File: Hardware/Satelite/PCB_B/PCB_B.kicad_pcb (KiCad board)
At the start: 2 copper layers, 54 x 54 mm, 66 parts, among them IC1 MCP1642B-50I_MS, IC2 MCP1642B-50I_MS, J1 Conector_PCB_B-C, J2 Conector_PCB_A-B, U1 MIC5323-3.3YD5_TR, U2 ADP2108AUJ-3.3, U3 INA194, U4 MCP6001-OT, U5 INA194, U6 MCP6001-OT, U7 INA194, U8 BQ24091DGQT, U9 BQ27441DRZR-G1A

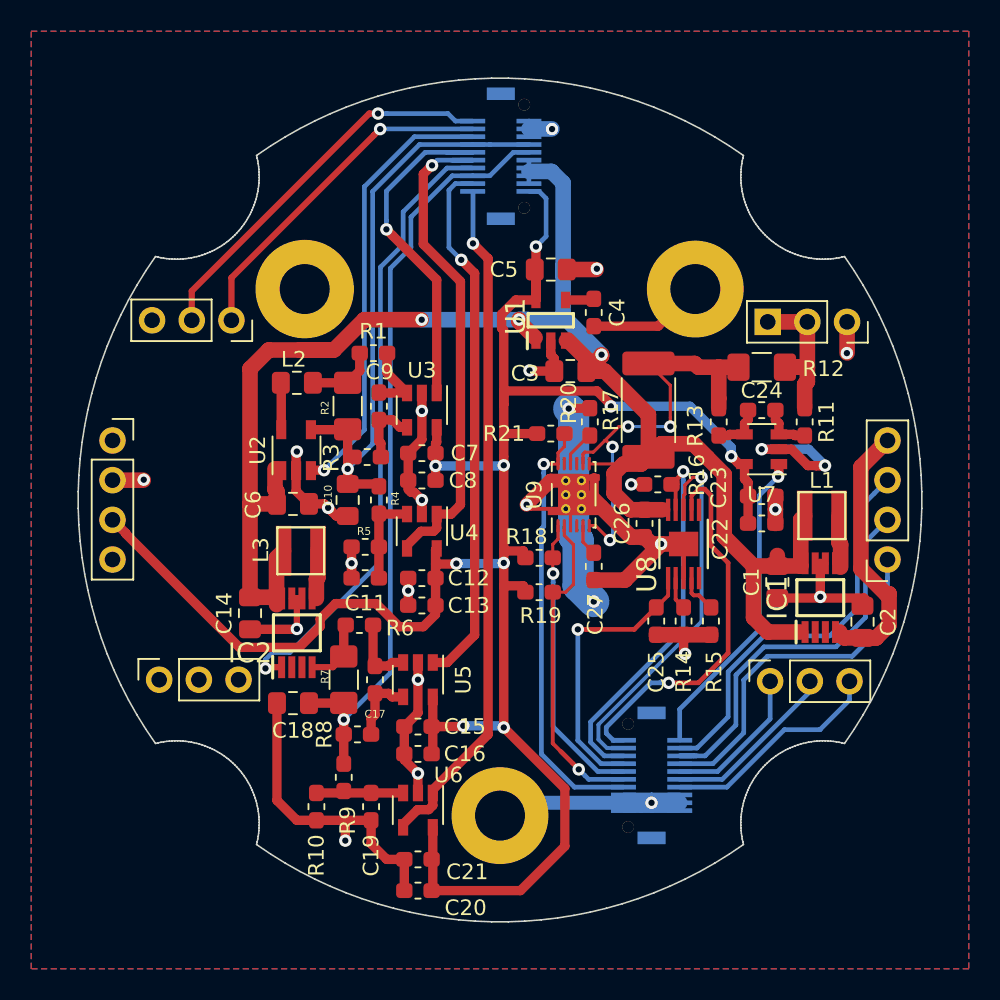
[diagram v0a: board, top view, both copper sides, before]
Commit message: Correciones de anchos de trazas en PCB B
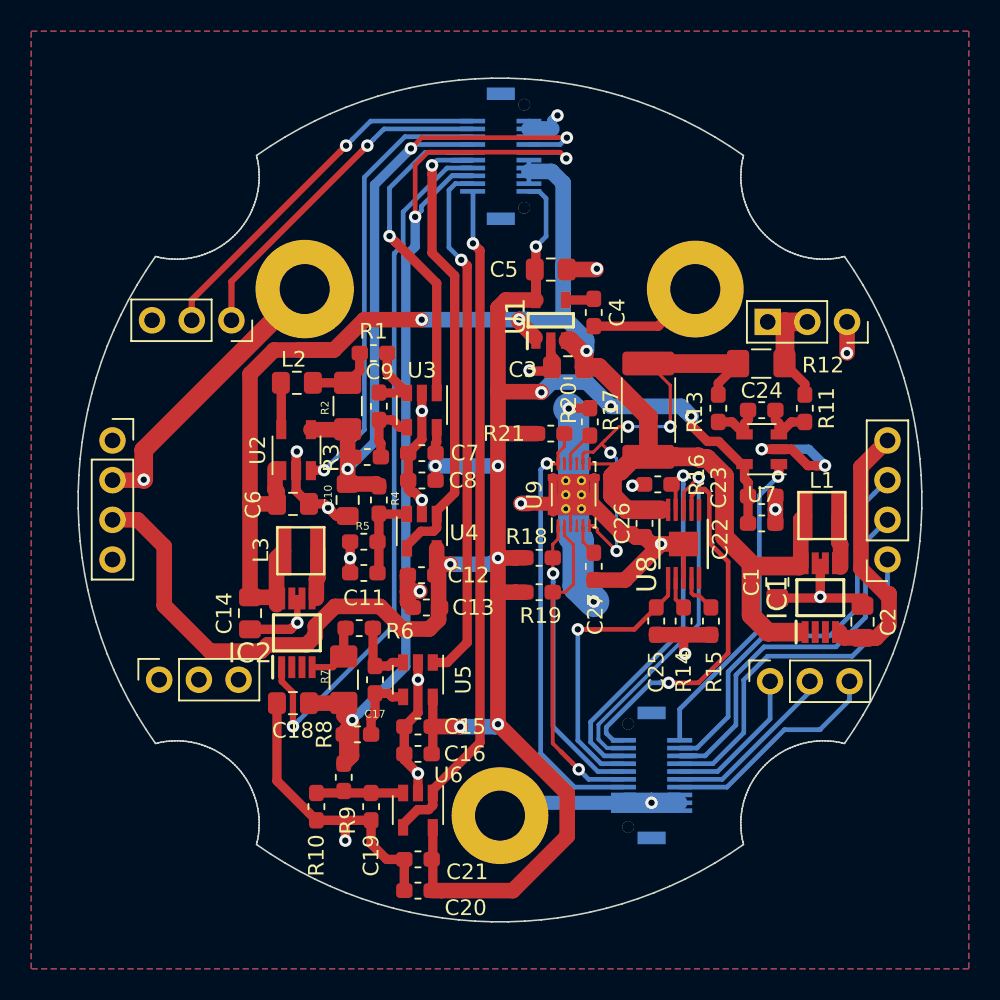
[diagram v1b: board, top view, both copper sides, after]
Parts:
- moved R13 0.87 mm to (14.0, -5.87)
- moved R11 0.87 mm to (19.5, -5.87)
- moved C11 0.34 mm to (-8.71, 4.67)
- moved R5 0.34 mm to (-8.71, 2.67)
- moved C13 0.32 mm to (-4.71, 6.88)
- moved C3 0.28 mm to (4.35, -8.49)
- moved R12 0.23 mm to (16.7, -8.73)
- moved R6 0.20 mm to (-9.01, 8.20)
- moved C12 0.19 mm to (-5.02, 4.81)
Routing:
- net GND: track 179.7 -> 199.0 mm
- net +5V: track 49.3 -> 66.5 mm, vias 1 -> 3
- net +3V3: track 38.0 -> 50.9 mm, vias 1 -> 3
- net +BATT: track 122.7 -> 114.3 mm
- net /ENABLE_5V: track 40.2 -> 45.5 mm
- net +3V3_Internal: track 140.7 -> 145.0 mm, vias 9 -> 10
- net /BATT_INTERNO: track 9.57 -> 7.97 mm
- net /Fuel Gauge/VBAT: track 28.7 -> 30.1 mm
- net /V_SENSE_3V3: track 32.2 -> 30.9 mm
- net /GPS_TX: track 24.8 -> 24.0 mm

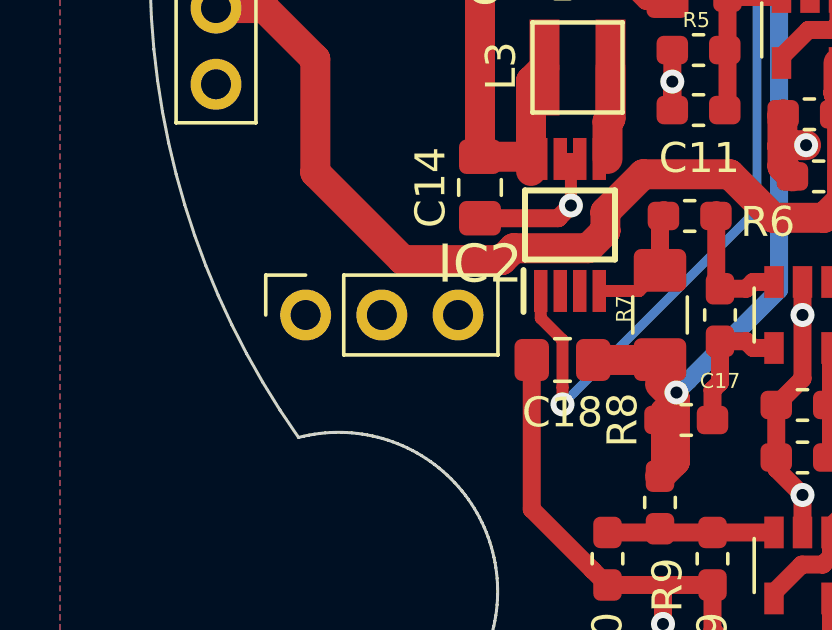
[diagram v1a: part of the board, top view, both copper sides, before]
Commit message: Eliminados pines no usados del conector A-B
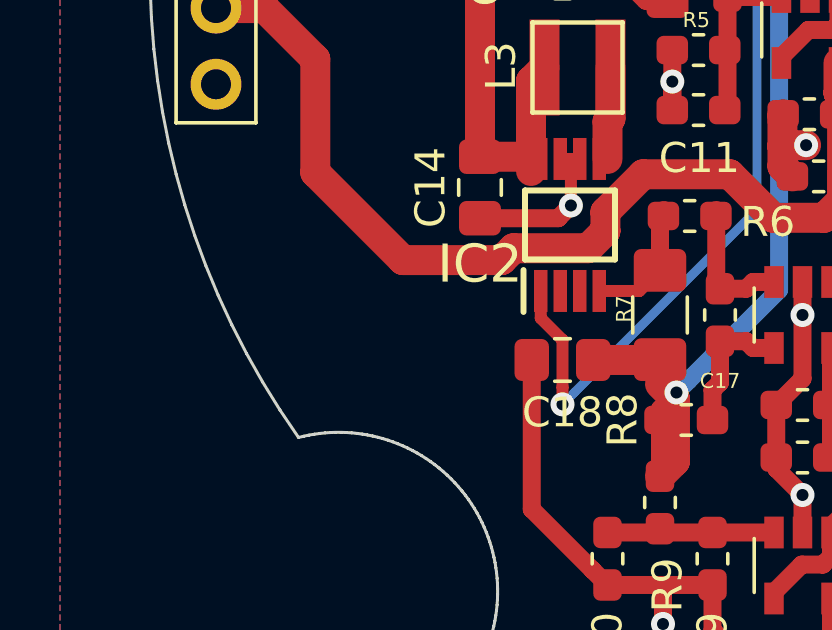
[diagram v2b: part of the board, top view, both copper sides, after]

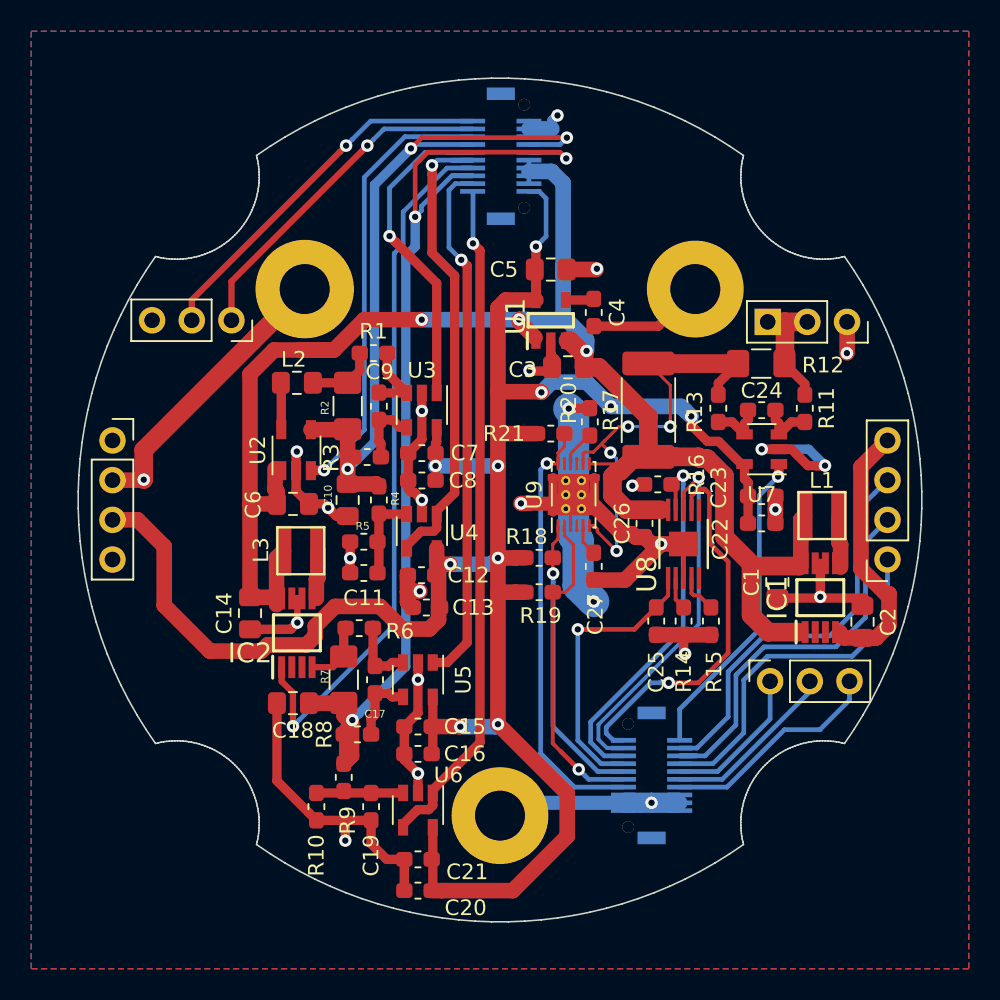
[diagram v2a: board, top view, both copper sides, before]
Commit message: Modificado conector A-B para poder alojar la batería entre A y B
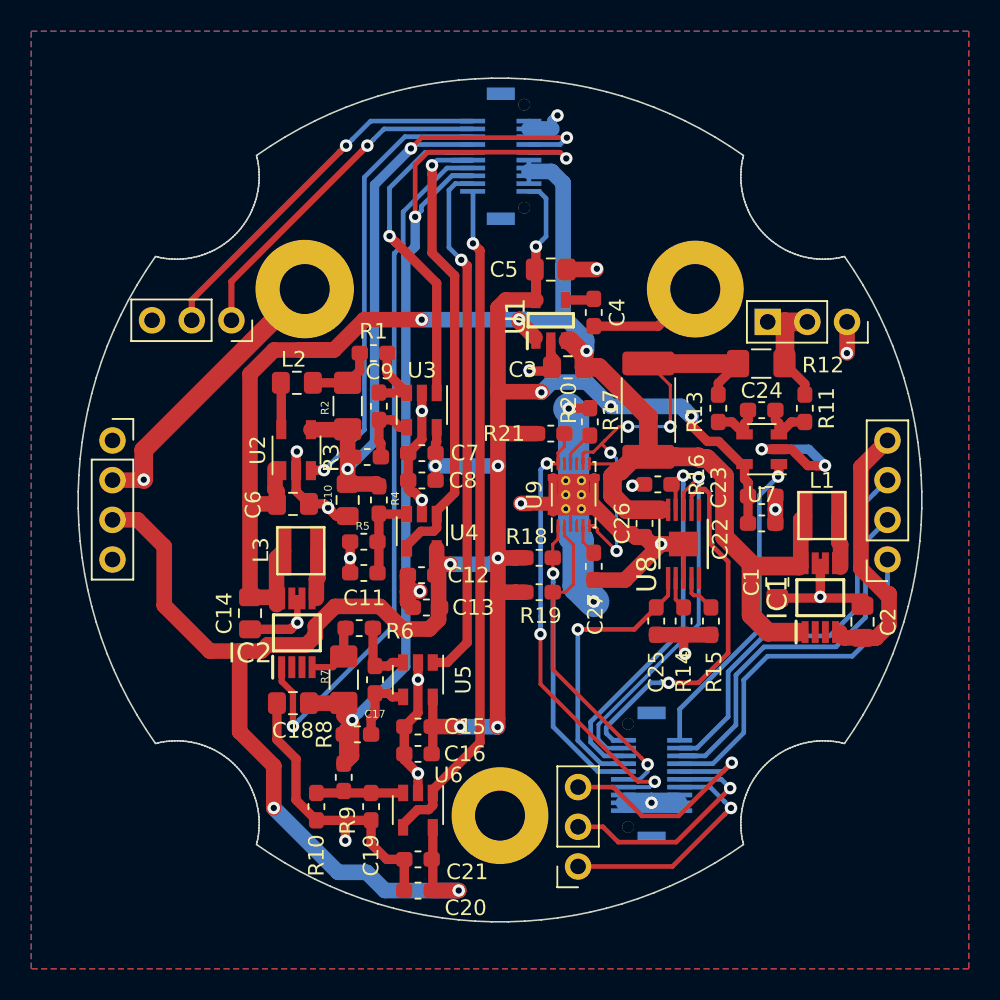
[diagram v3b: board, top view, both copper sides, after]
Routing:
- net GND: track 199.0 -> 190.1 mm
- net +3V3_Internal: track 145.0 -> 152.7 mm, vias 10 -> 12
- net /SCLK: track 9.59 -> 15.6 mm, vias 0 -> 1
- net /CS: track 11.3 -> 15.0 mm, vias 0 -> 1
- net /GPOUT: track 27.7 -> 29.2 mm, vias 1 -> 3
- net /SCL: track 22.7 -> 21.7 mm
- net /SDI: track 14.4 -> 15.2 mm, vias 0 -> 1
